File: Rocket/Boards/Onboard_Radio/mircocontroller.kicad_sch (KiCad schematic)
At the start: 21 parts, among them J4 USB_B_Micro, J5 SWD JST PH, U3 STM32G0B1RCTx, U8 STM32H562RGT6, Y1 12MHz

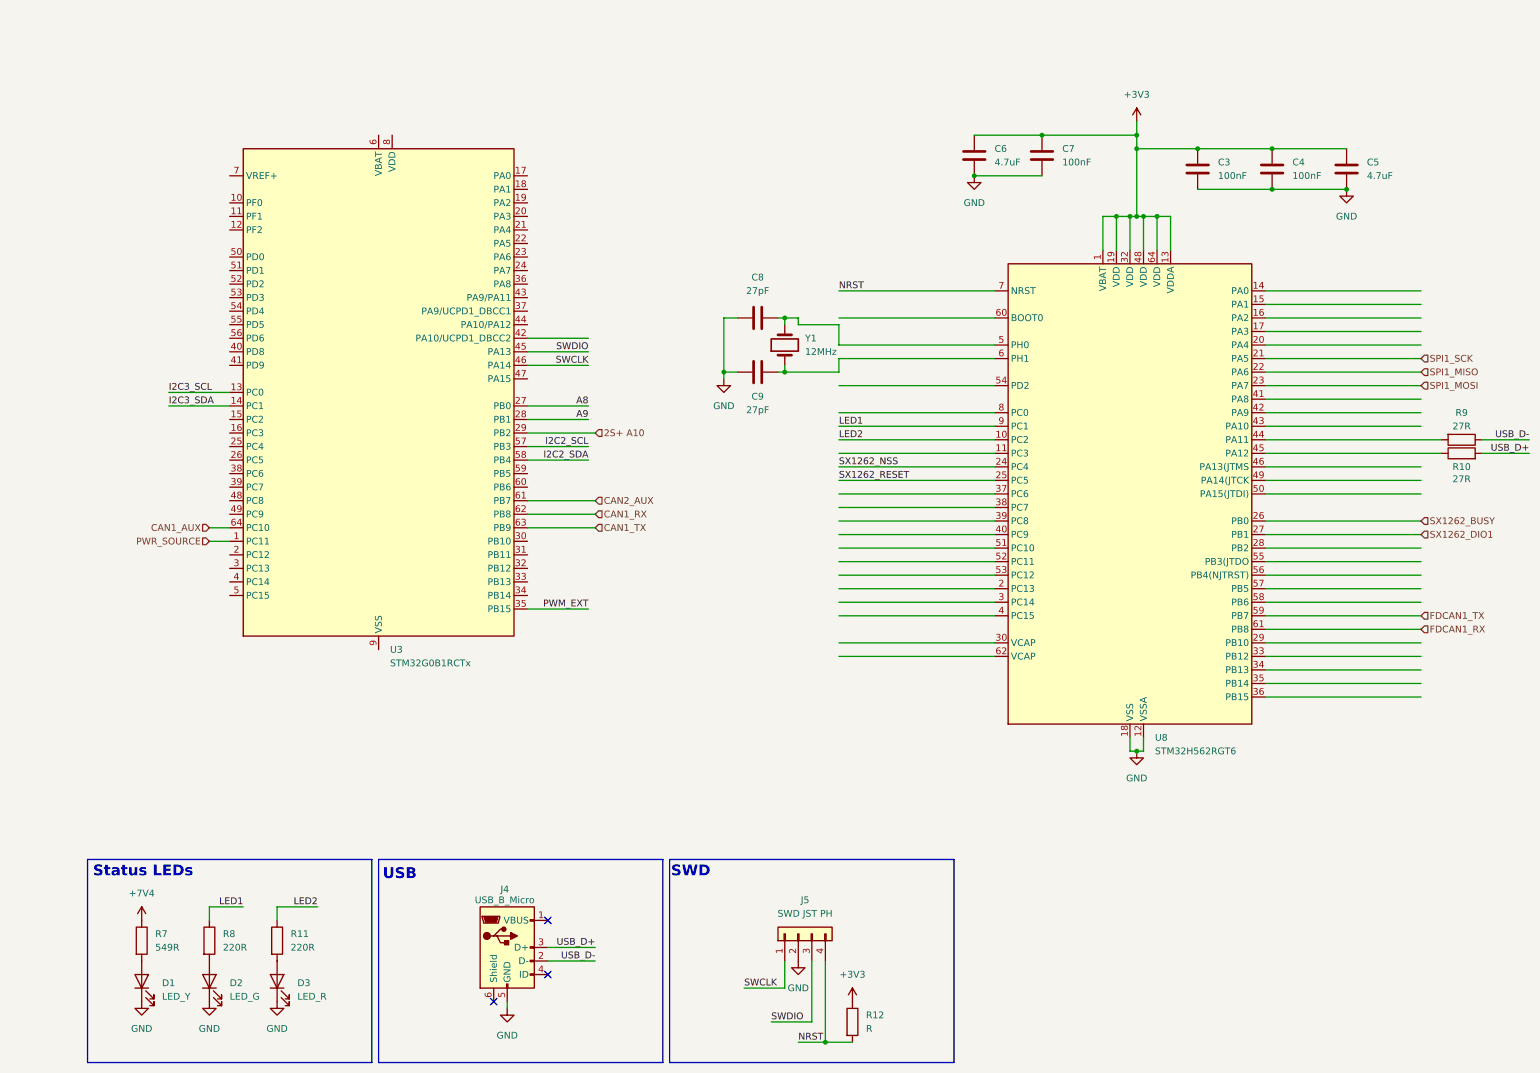
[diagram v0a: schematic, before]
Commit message: rf chip schematic changed
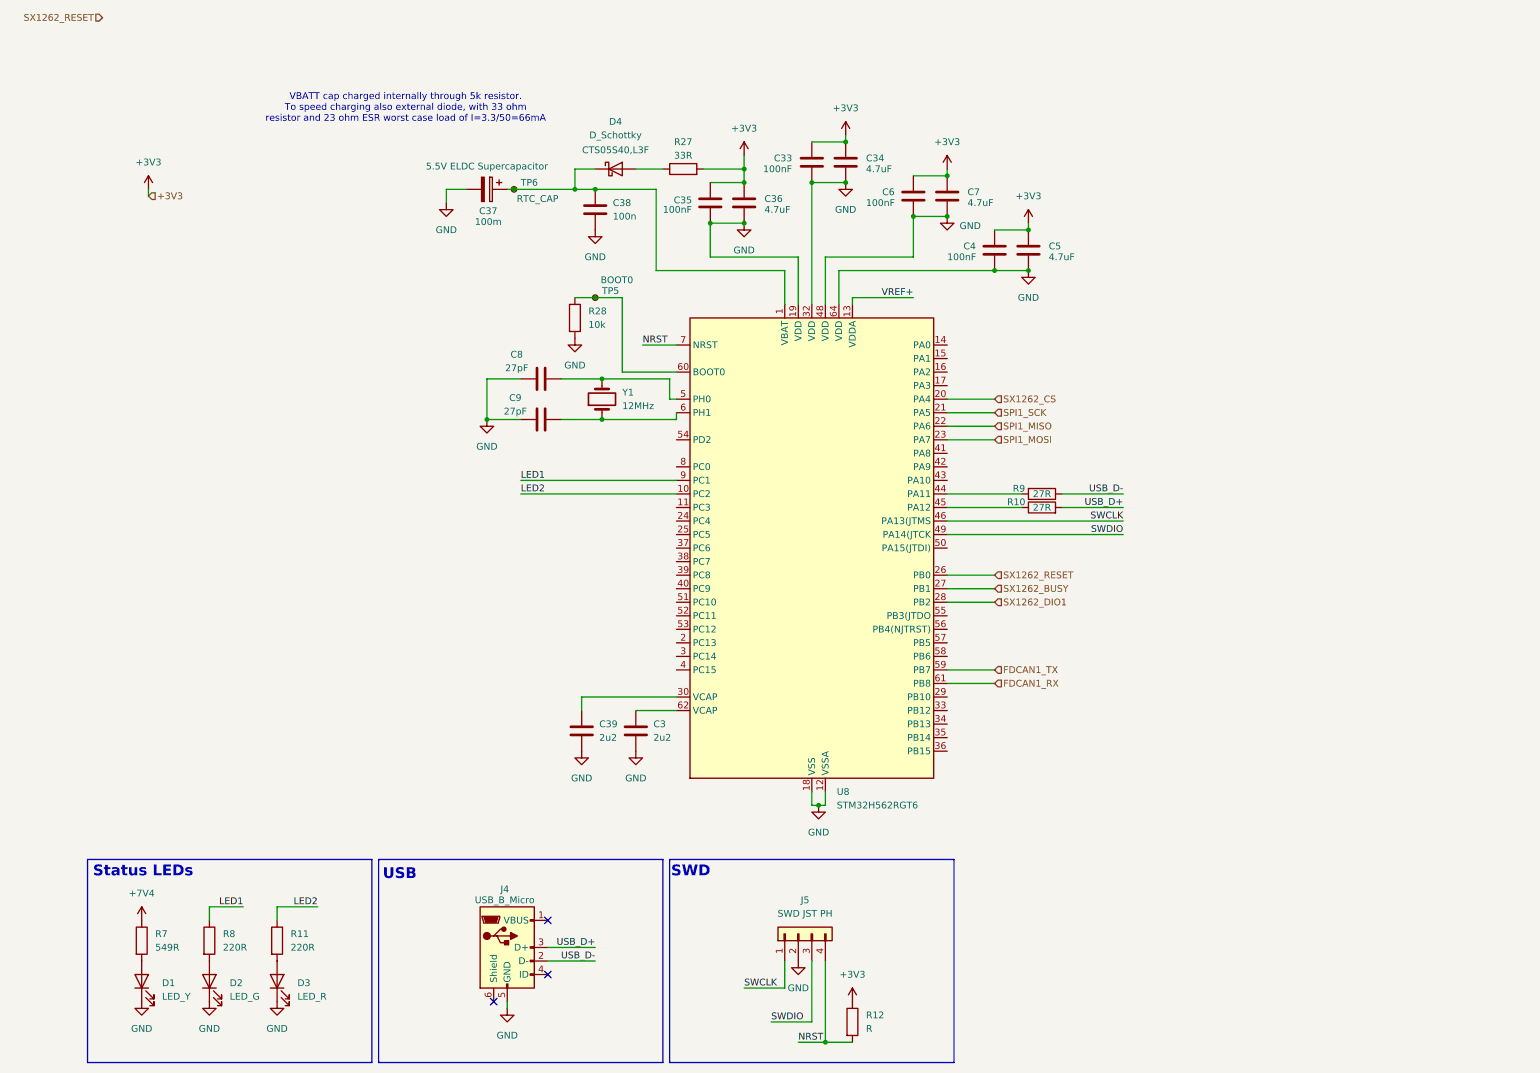
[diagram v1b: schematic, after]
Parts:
- removed U3: STM32G0B1RCTx, Package_QFP:LQFP-64_10x10mm_P0.5mm, symbol MCU_ST_STM32G0:STM32G0B1RCTx
- added C33, C35: 100nF, Capacitor_SMD:C_0603_1608Metric, symbol Device:C
- added C34, C36: 4.7uF, Capacitor_SMD:C_0603_1608Metric, symbol Device:C
- added C37: 100m, Capacitor_THT:CP_Radial_D14.0mm_P5.00mm, symbol Device:C_Polarized
- added C38: 100n, Capacitor_SMD:C_0402_1005Metric, symbol Device:C
- added C39: 2u2, symbol Device:C
- added D4: D_Schottky, Diode_SMD:D_SOD-882, symbol Device:D_Schottky
- added R27: 33R, Resistor_SMD:R_0603_1608Metric, symbol Device:R
- added R28: 10k, symbol Device:R
- added TP5: BOOT0, symbol Connector:TestPoint_Small
- added TP6: RTC_CAP, TestPoint:TestPoint_Pad_1.5x1.5mm, symbol Connector:TestPoint_Small
- C3: value 100nF -> 2u2; footprint Capacitor_SMD:C_0603_1608Metric -> (none); MPN CL10E104KC8VPNC -> (none); Manufacturer Samsung Electro-Mechanics -> (none); Max Temp 150 -> (none); Min Temp -55 -> (none); Voltage 100V -> (none)
- C6: value 4.7uF -> 100nF; MPN GRT188C81E475KE13D -> CL10E104KC8VPNC; Manufacturer Murata Electronics -> Samsung Electro-Mechanics; Max Temp 105 -> 150; Voltage 25V -> 100V
- C7: value 100nF -> 4.7uF; MPN CL10E104KC8VPNC -> GRT188C81E475KE13D; Manufacturer Samsung Electro-Mechanics -> Murata Electronics; Max Temp 150 -> 105; Voltage 100V -> 25V
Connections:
- net +3V3: now also C33.1, C34.1, C35.1, C36.1, R27.2; no longer C3.1, U8.1 (VBAT), U8.13 (VDDA), U8.19 (VDD), U8.32 (VDD), U8.48 (VDD), U8.64 (VDD)
- net GND: now also U8.19 (VDD), U8.32 (VDD), U8.48 (VDD), U8.64 (VDD), C33.2, C34.2, C35.2, C36.2, C37.2, C38.2, C39.2, R28.2
- net SWCLK: now also U8.46 (PA13(JTMS)
- net SWDIO: now also U8.49 (PA14(JTCK)
- net SX1262_BUSY: now also U8.27 (PB1); no longer U8.26 (PB0)
- net SX1262_DIO1: now also U8.28 (PB2); no longer U8.27 (PB1)
- net SX1262_RESET: now also U8.26 (PB0); no longer U8.25 (PC5)
- net SX1262_CS: now reaches U8.20 (PA4)
- net at U8.30 (VCAP): now also C39.1
- net at U8.60 (BOOT0): now also R28.1, TP5.1
- net at U8.62 (VCAP): now also C3.1
- net SX1262_NSS: no longer names the net of U8.24 (PC4)
- new net: C37.1, C38.1, D4.1 (K), TP6.1, U8.1 (VBAT)
- new net: D4.2 (A), R27.1
- new net VREF+: U8.13 (VDDA)
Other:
- note added: "VBATT cap charged internally through 5k resistor. To speed charging also external diode, with 33 ohm resistor and 23 ohm ESR worst case load of I=3.3/50=66mA"
- moved on the sheet: C4, C5, C8, C9, R10, R9, U8, Y1
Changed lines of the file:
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@@
 (kicad_sch
-	(version 20250114)
+	(version 20260306)
 	(generator "eeschema")
-	(generator_version "9.0")
+	(generator_version "10.0")
 	(paper "A4")
 	(title_block
